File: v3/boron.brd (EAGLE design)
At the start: 61 x 61 mm, 48 parts, among them J1 batt, J10 USB_MINI-B_SMT, J11 drv, J12 out, J13 RASM722, J14 debug, J16 5V, J4 ISP, Q1 Si7137DP, U2_C2 2.2uF, U2_L1 1 kOhm @ 100MHz, U2_L2 1 kOhm @ 100MHz, U2_R1 10k, U2_R2 10k, U2_R9 100K Ohms, U3 ATTINY84-20MU, U6 TPS61230A, U6_CBST 10 nF, U6_CFF 10pF, U6_CIN 22uF, U6_COUT 22uF, U6_RFBB 100K Ohms, U6_RFBT 316K Ohms, U9 BQ24168RGET, U9_C2 4.7uF, U9_C4 47uF, U9_C5 10nF, U9_C6 4.7uF, U9_L1 DR73-2R2-R

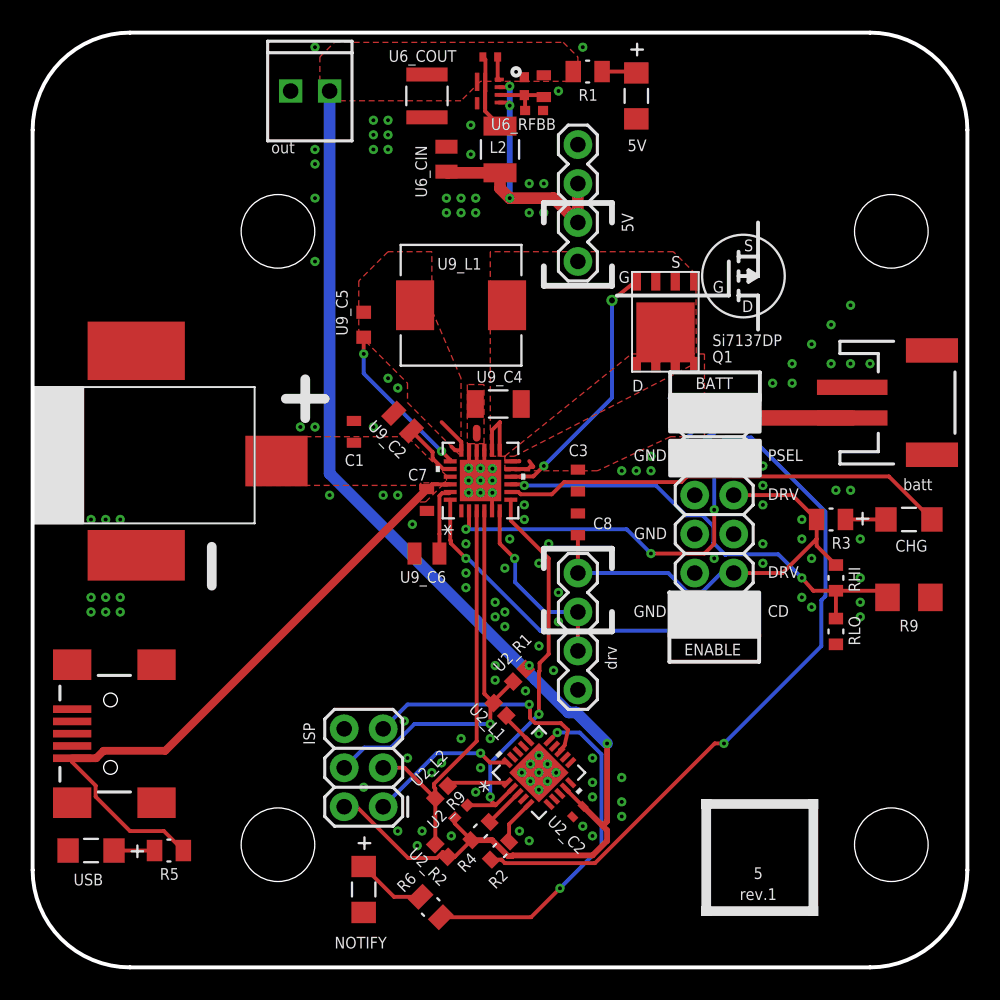
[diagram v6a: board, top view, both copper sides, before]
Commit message: Fixing the stupid backwards USB port.
Doh!
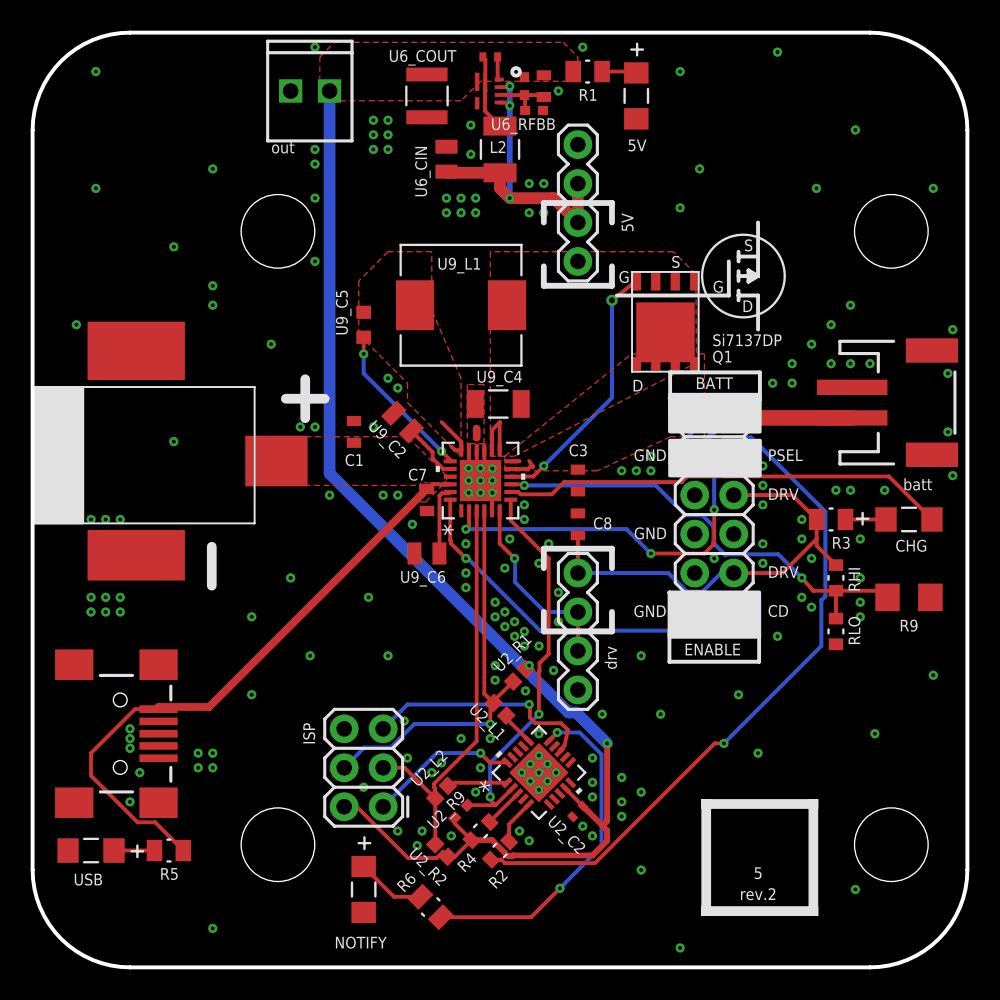
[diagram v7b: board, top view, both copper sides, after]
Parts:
- 5: value rev.1 -> rev.2
- moved J10 0.63 mm to (5.71, 15.2), turned to 0 degrees
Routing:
- net U9_USB: track 42.4 -> 40.3 mm
- net GND: vias 135 -> 188
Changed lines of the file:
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@@
 <setting verticaltext="up"/>
 </settings>
-<grid distance="0.05" unitdist="inch" unit="inch" style="lines" multiple="1" display="yes" altdistance="0.001" altunitdist="inch" altunit="inch"/>
+<grid distance="0.05" unitdist="inch" unit="inch" style="lines" multiple="1" display="yes" altdistance="0.0125" altunitdist="inch" altunit="inch"/>
 <layers>
 <layer number="1" name="Top" color="4" fill="1" visible="yes" active="yes"/>
@@
 <layer number="19" name="Unrouted" color="6" fill="1" visible="yes" active="yes"/>
 <layer number="20" name="Dimension" color="15" fill="1" visible="yes" active="yes"/>
-<layer number="21" name="tPlace" color="7" fill="1" visible="no" active="yes"/>
-<layer number="22" name="bPlace" color="7" fill="1" visible="yes" active="yes"/>
+<layer number="21" name="tPlace" color="7" fill="1" visible="yes" active="yes"/>
+<layer number="22" name="bPlace" color="7" fill="1" visible="no" active="yes"/>
 <layer number="23" name="tOrigins" color="15" fill="1" visible="yes" active="yes"/>
 <layer number="24" name="bOrigins" color="15" fill="1" visible="yes" active="yes"/>
@@
 <attribute name="VENDOR" value="Texas Instruments" x="29.21" y="31.75" size="1.778" layer="27" rot="R90" display="off"/>
 </element>
-<element name="J10" library="SparkFun-Connectors" package="USB-MINIB" value="USB_MINI-B_SMT" x="5.08" y="15.24" smashed="yes" rot="R180">
-<attribute name="PROD_ID" value="CONN-08193" x="5.08" y="15.24" size="1.778" layer="27" rot="R180" display="off"/>
-<attribute name="SF_ID" value="PRT-00587" x="5.08" y="15.24" size="1.778" layer="27" rot="R180" display="off"/>
+<element name="J10" library="SparkFun-Connectors" package="USB-MINIB" value="USB_MINI-B_SMT" x="5.715" y="15.24" smashed="yes">
+<attribute name="PROD_ID" value="CONN-08193" x="5.715" y="15.24" size="1.778" layer="27" display="off"/>
+<attribute name="SF_ID" value="PRT-00587" x="5.715" y="15.24" size="1.778" layer="27" display="off"/>
 </element>
 <element name="J4" library="SparkFun-Connectors" package="2X3" value="ISP" x="22.86" y="10.4775" smashed="yes" rot="R90">
@@
 <attribute name="VALUE" value="FEMALE 2x3" x="22.86" y="10.4775" size="1.778" layer="27" rot="R90" display="off"/>
 </element>
-<element name="5" library="32bits" package="PERIODIC_SYMBOL_BACK" value="rev.1" x="49.9624" y="4.6228" rot="MR0">
+<element name="5" library="32bits" package="PERIODIC_SYMBOL_BACK" value="rev.2" x="49.9624" y="4.6228" rot="MR0">
 <attribute name="ELEMENT" value="B" x="47.4224" y="7.1628" size="0.762" layer="25" ratio="20" align="bottom-center" display="off"/>
 </element>
@@
 <via x="34.1376" y="12.7" extent="1-16" drill="0.254"/>
 <via x="33.02" y="11.5824" extent="1-16" drill="0.254"/>
+<via x="6.35" y="15.5575" extent="1-16" drill="0.254"/>
+<via x="6.35" y="14.2875" extent="1-16" drill="0.254"/>
+<via x="6.985" y="12.7" extent="1-16" drill="0.254"/>
+<via x="6.35" y="10.795" extent="1-16" drill="0.254"/>
+<via x="10.795" y="13.97" extent="1-16" drill="0.254"/>
+<via x="10.795" y="13.0175" extent="1-16" drill="0.254"/>
+<via x="11.7475" y="13.0175" extent="1-16" drill="0.254"/>
+<via x="11.7475" y="13.97" extent="1-16" drill="0.254"/>
+<via x="31.4325" y="22.5425" extent="1-16" drill="0.254"/>
+<via x="31.4325" y="21.59" extent="1-16" drill="0.254"/>
+<via x="32.0675" y="21.9075" extent="1-16" drill="0.254"/>
+<via x="32.0675" y="20.955" extent="1-16" drill="0.254"/>
+<via x="6.35" y="14.9225" extent="1-16" drill="0.254"/>
+<via x="55.5625" y="31.115" extent="1-16" drill="0.254"/>
+<via x="59.69" y="38.735" extent="1-16" drill="0.254"/>
+<via x="59.69" y="34.925" extent="1-16" drill="0.254"/>
+<via x="60.0075" y="41.5925" extent="1-16" drill="0.254"/>
+<via x="60.0075" y="32.0675" extent="1-16" drill="0.254"/>
+<via x="14.2875" y="17.78" extent="1-16" drill="0.254"/>
+<via x="18.0975" y="20.32" extent="1-16" drill="0.254"/>
+<via x="23.1775" y="20.32" extent="1-16" drill="0.254"/>
+<via x="21.9075" y="24.13" extent="1-16" drill="0.254"/>
+<via x="9.2075" y="34.29" extent="1-16" drill="0.254"/>
+<via x="11.7475" y="2.54" extent="1-16" drill="0.254"/>
+<via x="39.6875" y="6.35" extent="1-16" drill="0.254"/>
+<via x="47.3075" y="13.97" extent="1-16" drill="0.254"/>
+<via x="53.6575" y="5.08" extent="1-16" drill="0.254"/>
+<via x="42.2275" y="1.27" extent="1-16" drill="0.254"/>
+<via x="58.7375" y="19.05" extent="1-16" drill="0.254"/>
+<via x="54.9275" y="15.24" extent="1-16" drill="0.254"/>
+<via x="2.8575" y="41.91" extent="1-16" drill="0.254"/>
+<via x="4.1275" y="50.8" extent="1-16" drill="0.254"/>
+<via x="4.1275" y="58.42" extent="1-16" drill="0.254"/>
+<via x="11.7475" y="52.07" extent="1-16" drill="0.254"/>
+<via x="9.2075" y="46.99" extent="1-16" drill="0.254"/>
+<via x="11.7475" y="44.45" extent="1-16" drill="0.254"/>
+<via x="11.7475" y="43.18" extent="1-16" drill="0.254"/>
+<via x="15.5575" y="40.64" extent="1-16" drill="0.254"/>
+<via x="48.5775" y="59.69" extent="1-16" drill="0.254"/>
+<via x="58.7375" y="50.8" extent="1-16" drill="0.254"/>
+<via x="51.1175" y="50.8" extent="1-16" drill="0.254"/>
+<via x="53.6575" y="54.61" extent="1-16" drill="0.254"/>
+<via x="42.2275" y="49.53" extent="1-16" drill="0.254"/>
+<via x="43.4975" y="52.07" extent="1-16" drill="0.254"/>
+<via x="42.2275" y="58.42" extent="1-16" drill="0.254"/>
+<via x="48.5775" y="21.59" extent="1-16" drill="0.254"/>
+<via x="39.6875" y="20.32" extent="1-16" drill="0.254"/>
+<via x="37.1475" y="16.51" extent="1-16" drill="0.254"/>
+<via x="40.9575" y="16.51" extent="1-16" drill="0.254"/>
+<via x="46.0375" y="17.78" extent="1-16" drill="0.254"/>
+<via x="39.6875" y="11.43" extent="1-16" drill="0.254"/>
+<via x="14.2875" y="22.86" extent="1-16" drill="0.254"/>
+<via x="16.8275" y="25.4" extent="1-16" drill="0.254"/>
 </signal>
 <signal name="VBAT">
@@
 <contactref element="C7" pad="1"/>
 <contactref element="R5" pad="2"/>
-<wire x1="4.1094" y1="11.85573125" x2="4.1094" y2="11.1306" width="0.254" layer="1"/>
-<wire x1="4.1094" y1="11.1306" x2="6.35" y2="8.89" width="0.254" layer="1"/>
-<wire x1="2.58" y1="13.38513125" x2="2.58" y2="13.64" width="0.254" layer="1"/>
-<wire x1="2.58" y1="13.38513125" x2="4.1094" y2="11.85573125" width="0.254" layer="1"/>
-<wire x1="6.35" y1="8.89" x2="8.5598" y2="8.89" width="0.254" layer="1"/>
-<wire x1="8.5598" y1="8.89" x2="9.8298" y2="7.62" width="0.254" layer="1"/>
 <wire x1="27.235" y1="31.4999375" x2="26.0262375" y2="31.4999375" width="0.254" layer="1"/>
 <wire x1="25.7175" y1="31.1912" x2="26.0262375" y2="31.4999375" width="0.254" layer="1"/>
-<wire x1="2.58" y1="13.64" x2="4.145575" y2="13.64" width="0.508" layer="1"/>
-<wire x1="4.145575" y1="13.64" x2="4.630575" y2="14.125" width="0.508" layer="1"/>
-<wire x1="8.6513" y1="14.125" x2="25.7175" y2="31.1912" width="0.508" layer="1"/>
-<wire x1="4.630575" y1="14.125" x2="8.6513" y2="14.125" width="0.508" layer="1"/>
+<wire x1="25.7175" y1="31.1912" x2="11.5088" y2="16.9825" width="0.508" layer="1"/>
 <polygon width="0.1524" layer="1" thermals="no">
 <vertex x="25.2476" y="30.353"/>
@@
 <vertex x="25.2476" y="31.496"/>
 </polygon>
+<wire x1="11.5088" y1="16.9825" x2="8.215" y2="16.9825" width="0.508" layer="1"/>
+<wire x1="8.215" y1="16.9825" x2="8.215" y2="16.84" width="0.508" layer="1"/>
+<wire x1="8.215" y1="16.84" x2="6.68" y2="16.84" width="0.254" layer="1"/>
+<wire x1="6.68" y1="16.84" x2="3.81" y2="13.97" width="0.254" layer="1"/>
+<wire x1="6.84926875" y1="9.4606" x2="7.9892" y2="9.4606" width="0.254" layer="1"/>
+<wire x1="7.9892" y1="9.4606" x2="9.8298" y2="7.62" width="0.254" layer="1"/>
+<wire x1="3.81" y1="13.97" x2="3.81" y2="12.49986875" width="0.254" layer="1"/>
+<wire x1="3.81" y1="12.49986875" x2="6.84926875" y2="9.4606" width="0.254" layer="1"/>
 </signal>
 <signal name="U9_STAT">

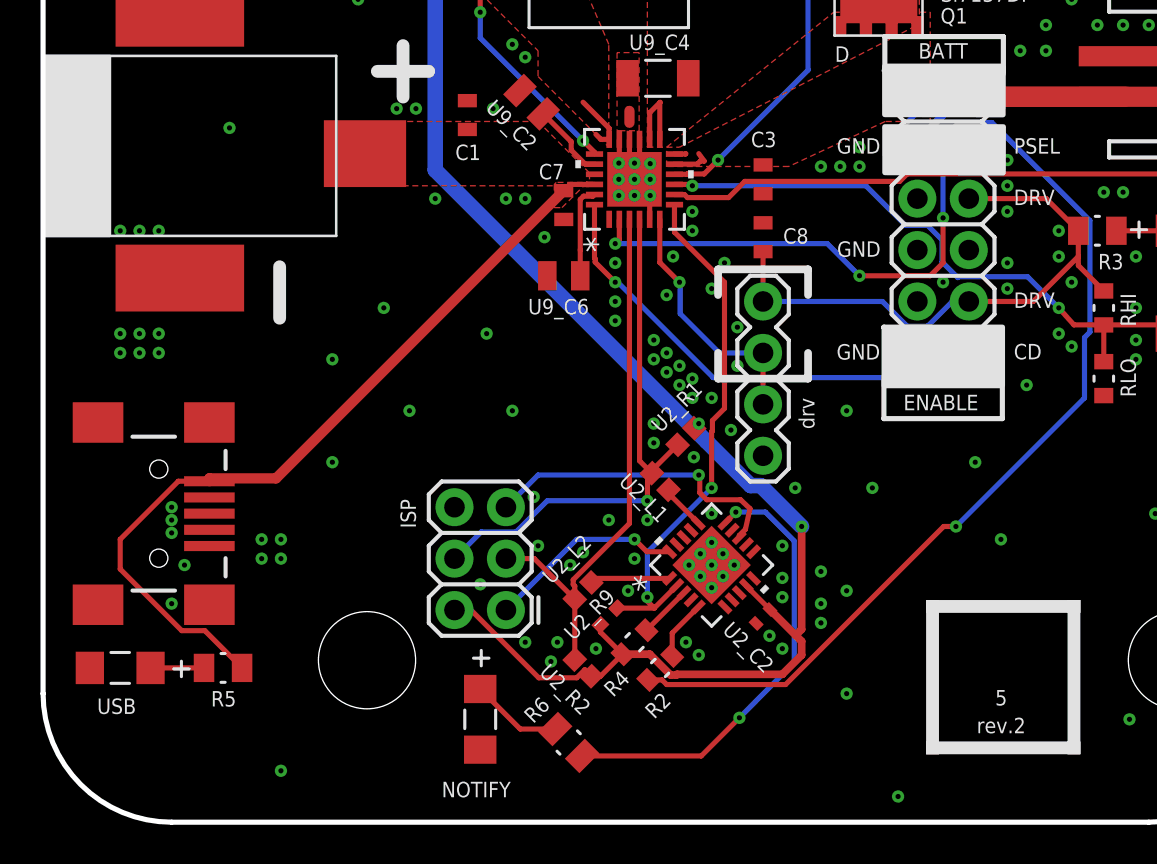
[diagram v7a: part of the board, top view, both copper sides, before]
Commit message: Boron R.3 off to osh park.
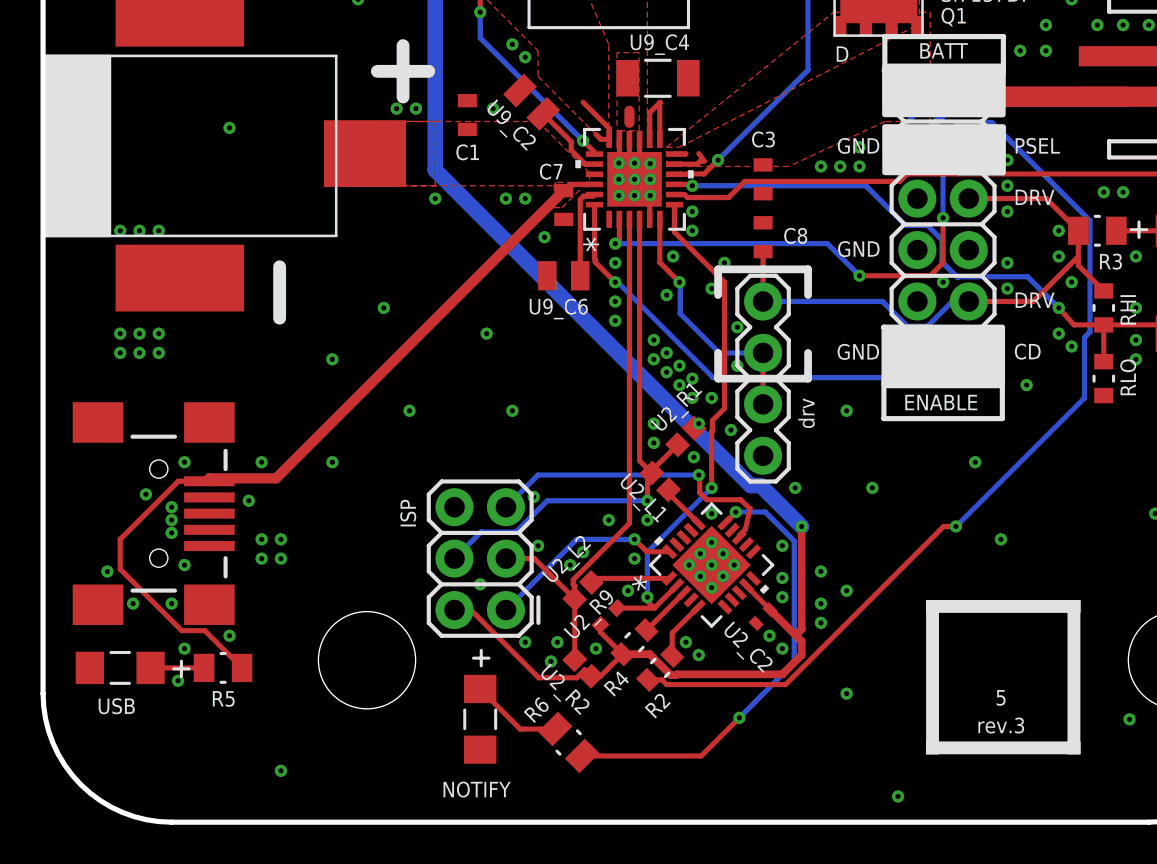
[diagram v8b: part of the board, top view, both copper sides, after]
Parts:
- 5: value rev.2 -> rev.3
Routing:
- net GND: vias 188 -> 197
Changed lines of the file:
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@@
 <attribute name="VALUE" value="FEMALE 2x3" x="22.86" y="10.4775" size="1.778" layer="27" rot="R90" display="off"/>
 </element>
-<element name="5" library="32bits" package="PERIODIC_SYMBOL_BACK" value="rev.2" x="49.9624" y="4.6228" rot="MR0">
+<element name="5" library="32bits" package="PERIODIC_SYMBOL_BACK" value="rev.3" x="49.9624" y="4.6228" rot="MR0">
 <attribute name="ELEMENT" value="B" x="47.4224" y="7.1628" size="0.762" layer="25" ratio="20" align="bottom-center" display="off"/>
 </element>
@@
 <via x="14.2875" y="22.86" extent="1-16" drill="0.254"/>
 <via x="16.8275" y="25.4" extent="1-16" drill="0.254"/>
+<via x="9.2075" y="9.2075" extent="1-16" drill="0.254"/>
+<via x="6.985" y="8.5725" extent="1-16" drill="0.254"/>
+<via x="6.6675" y="6.985" extent="1-16" drill="0.254"/>
+<via x="4.445" y="10.795" extent="1-16" drill="0.254"/>
+<via x="3.175" y="12.3825" extent="1-16" drill="0.254"/>
+<via x="10.795" y="17.78" extent="1-16" drill="0.254"/>
+<via x="6.985" y="17.78" extent="1-16" drill="0.254"/>
+<via x="5.08" y="16.1925" extent="1-16" drill="0.254"/>
+<via x="10.16" y="15.875" extent="1-16" drill="0.254"/>
 </signal>
 <signal name="VBAT">
@@
 <vertex x="24.4475" y="34.6075"/>
 </polygon>
-</signal>
+<polygon width="0.254" layer="1" thermals="no">
+<vertex x="16.8275" y="34.6075"/>
+<vertex x="19.3675" y="34.6075"/>
+<vertex x="19.3675" y="31.4325"/>
+<vertex x="16.8275" y="31.4325"/>
+<vertex x="16.8275" y="31.75"/>
+</polygon>
+</signal>
